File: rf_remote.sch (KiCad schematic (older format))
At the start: 21 parts, among them J1 10118194-0001LF, P1 CONN_01X04, P2 CONN_01X01, U1 SAMD21E18, U2 RFM69CW-915MHZ, U3 MIC5504-3.3YM5-T5

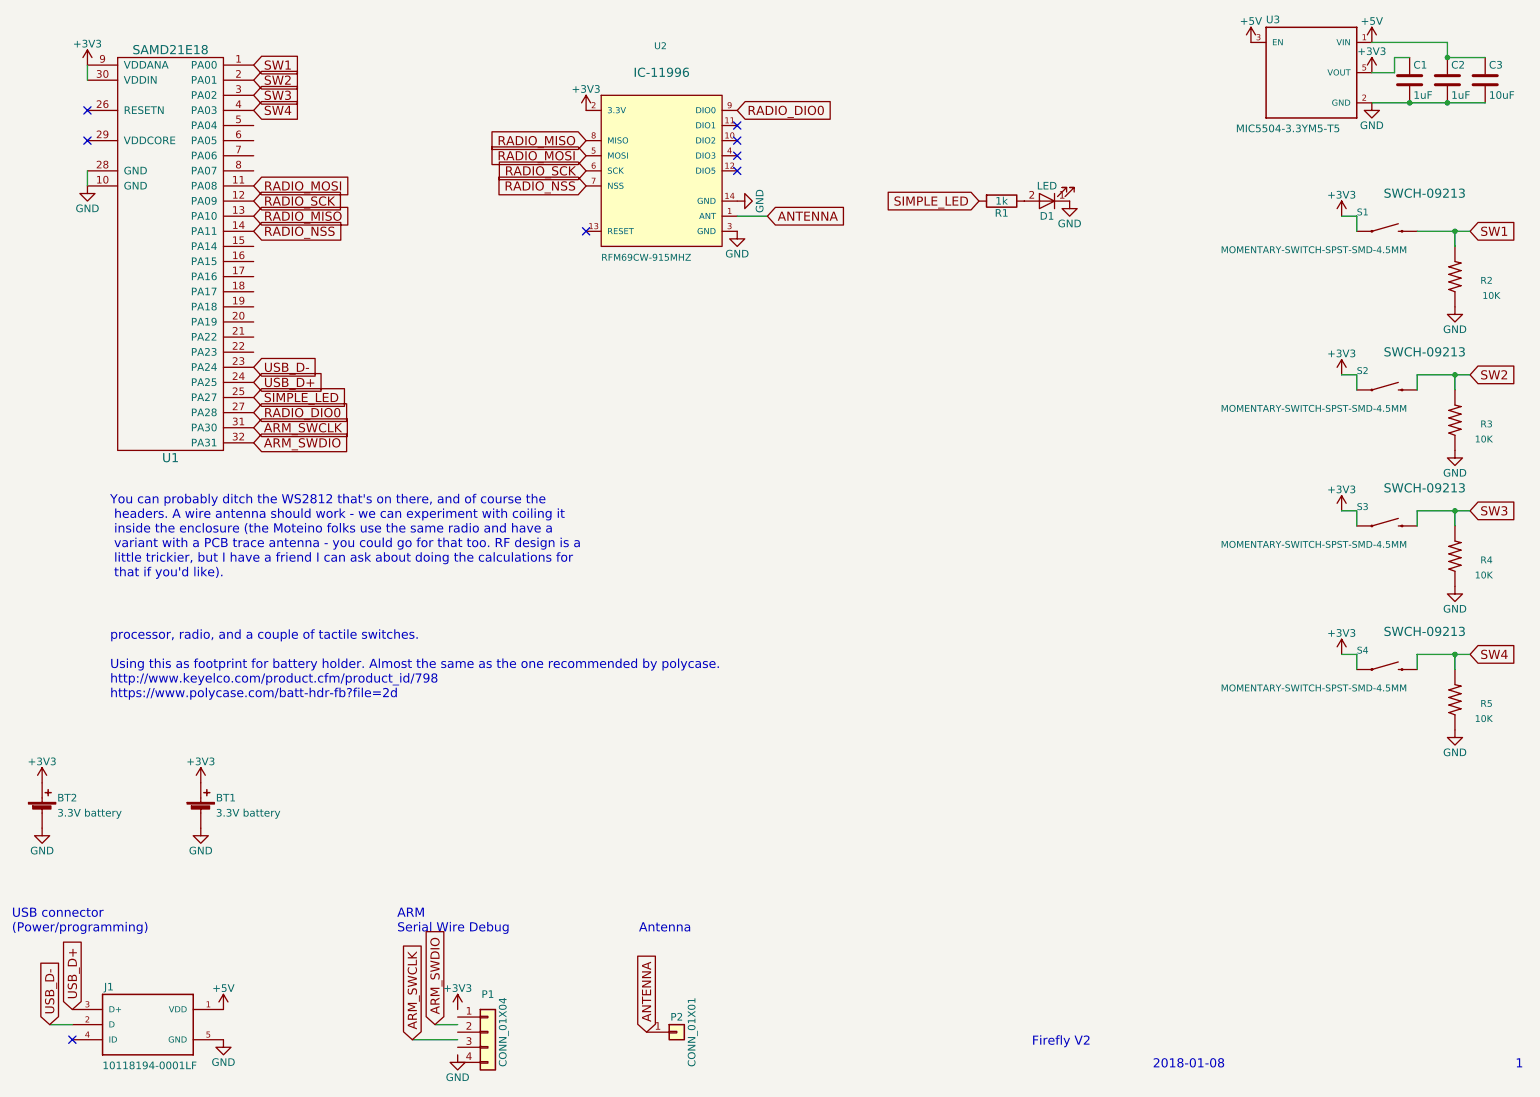
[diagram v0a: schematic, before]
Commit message: Removed second battery, updated PCB layout
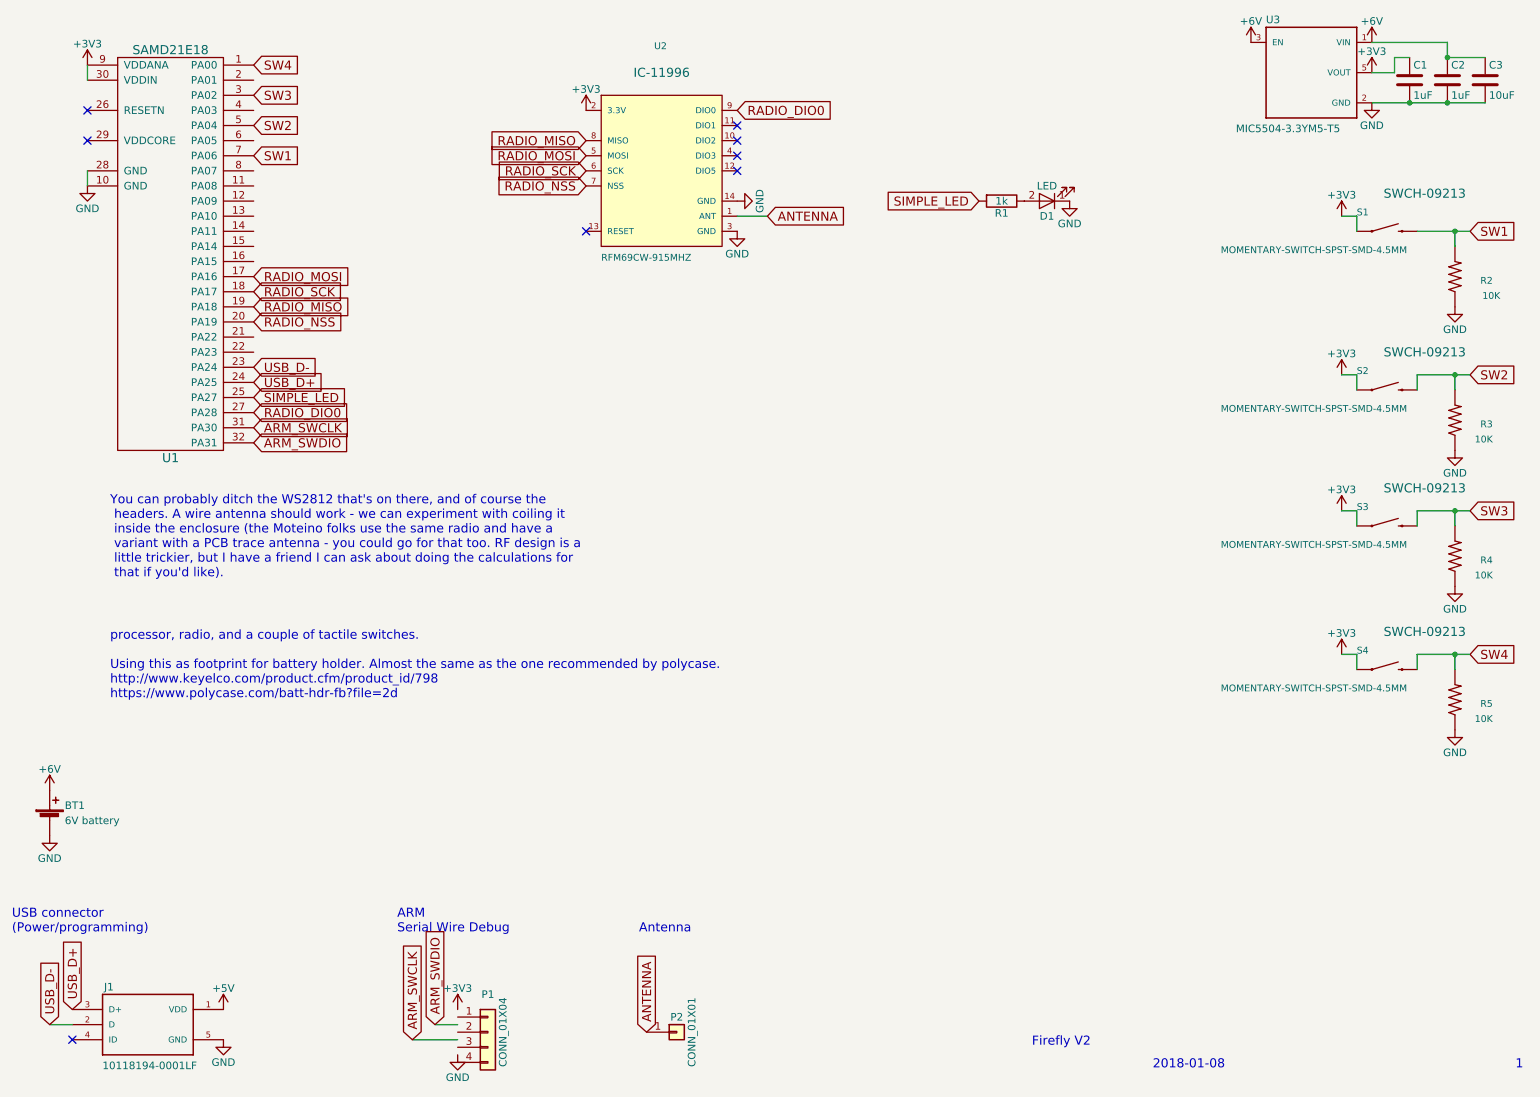
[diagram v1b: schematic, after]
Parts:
- removed BT2: 3.3V battery, Battery_Holders:Keystone_3034_1x20mm-CoinCell, symbol Battery_Cell
- BT1: value 3.3V battery -> 6V battery
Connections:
- net labels added: +6V
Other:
- moved on the sheet: BT1
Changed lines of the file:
@@
 $EndComp
 $Comp
-L +5V #PWR08
-U 1 1 5A547413
-P 8800 850
-F 0 "#PWR08" H 8800 700 50  0001 C CNN
-F 1 "+5V" H 8800 990 50  0000 C CNN
-F 2 "" H 8800 850 50  0000 C CNN
-F 3 "" H 8800 850 50  0000 C CNN
-	1    8800 850
-	1    0    0    -1
-$EndComp
-$Comp
-L +3V3 #PWR09
+L +3V3 #PWR08
 U 1 1 5A547441
 P 9600 1050
-F 0 "#PWR09" H 9600 900 50  0001 C CNN
+F 0 "#PWR08" H 9600 900 50  0001 C CNN
 F 1 "+3V3" H 9600 1190 50  0000 C CNN
 F 2 "" H 9600 1050 50  0000 C CNN
@@
 $EndComp
 $Comp
-L +3V3 #PWR010
+L +3V3 #PWR09
 U 1 1 5A54A758
 P 4400 1300
-F 0 "#PWR010" H 4400 1150 50  0001 C CNN
+F 0 "#PWR09" H 4400 1150 50  0001 C CNN
 F 1 "+3V3" H 4400 1440 50  0000 C CNN
 F 2 "" H 4400 1300 50  0000 C CNN
@@
 $EndComp
 $Comp
-L +5V #PWR011
-U 1 1 5A84FAAB
-P 9600 850
-F 0 "#PWR011" H 9600 700 50  0001 C CNN
-F 1 "+5V" H 9600 990 50  0000 C CNN
-F 2 "" H 9600 850 50  0000 C CNN
-F 3 "" H 9600 850 50  0000 C CNN
-	1    9600 850
-	1    0    0    -1
-$EndComp
-$Comp
 L C C1
 U 1 1 5A84FB7B
@@
 $EndComp
 $Comp
-L +3V3 #PWR012
+L +3V3 #PWR010
 U 1 1 5A851BC3
 P 1100 1000
-F 0 "#PWR012" H 1100 850 50  0001 C CNN
+F 0 "#PWR010" H 1100 850 50  0001 C CNN
 F 1 "+3V3" H 1100 1140 50  0000 C CNN
 F 2 "" H 1100 1000 50  0001 C CNN
@@
 	1100 1100 1100 1000
 $Comp
-L GND #PWR013
+L GND #PWR011
 U 1 1 5A851C44
 P 1100 1800
-F 0 "#PWR013" H 1100 1550 50  0001 C CNN
+F 0 "#PWR011" H 1100 1550 50  0001 C CNN
 F 1 "GND" H 1100 1650 50  0000 C CNN
 F 2 "" H 1100 1800 50  0001 C CNN
@@
 Text GLabel 2200 3100 2    60   Input ~ 0
 USB_D+
-Text GLabel 2200 1800 2    60   Input ~ 0
+Text GLabel 2200 2400 2    60   Input ~ 0
 RADIO_MOSI
-Text GLabel 2200 1900 2    60   Input ~ 0
+Text GLabel 2200 2500 2    60   Input ~ 0
 RADIO_SCK
-Text GLabel 2200 2000 2    60   Input ~ 0
+Text GLabel 2200 2600 2    60   Input ~ 0
 RADIO_MISO
-Text GLabel 2200 2100 2    60   Input ~ 0
+Text GLabel 2200 2700 2    60   Input ~ 0
 RADIO_NSS
 Text GLabel 2200 3200 2    60   Input ~ 0
@@
 SIMPLE_LED
 $Comp
-L GND #PWR014
+L GND #PWR012
 U 1 1 5A853737
 P 7600 1900
-F 0 "#PWR014" H 7600 1650 50  0001 C CNN
+F 0 "#PWR012" H 7600 1650 50  0001 C CNN
 F 1 "GND" H 7600 1750 50  0000 C CNN
 F 2 "" H 7600 1900 50  0000 C CNN
@@
 Text Notes 1250 5200 0    60   ~ 0
 processor, radio, and a couple of tactile switches.\n\nUsing this as footprint for battery holder. Almost the same as the one recommended by polycase.\nhttp://www.keyelco.com/product.cfm/product_id/798\nhttps://www.polycase.com/batt-hdr-fb?file=2d
-Text GLabel 2200 1000 2    60   Input ~ 0
+Text GLabel 2200 1600 2    60   Input ~ 0
 SW1
 Text GLabel 10250 2100 2    60   Input ~ 0
 SW1
-Text GLabel 2200 1100 2    60   Input ~ 0
+Text GLabel 2200 1400 2    60   Input ~ 0
 SW2
 Text GLabel 2200 1200 2    60   Input ~ 0
 SW3
-Text GLabel 2200 1300 2    60   Input ~ 0
+Text GLabel 2200 1000 2    60   Input ~ 0
 SW4
 Text GLabel 10250 3050 2    60   Input ~ 0
@@
 SW4
 $Comp
-L GND #PWR015
+L GND #PWR013
 U 1 1 5ADD2C56
 P 10150 2600
-F 0 "#PWR015" H 10150 2350 50  0001 C CNN
+F 0 "#PWR013" H 10150 2350 50  0001 C CNN
 F 1 "GND" H 10150 2450 50  0000 C CNN
 F 2 "" H 10150 2600 50  0001 C CNN
@@
 Connection ~ 10150 4900
 $Comp
-L +3V3 #PWR016
+L +3V3 #PWR014
 U 1 1 5ADD30DC
 P 9400 2000
-F 0 "#PWR016" H 9400 1850 50  0001 C CNN
+F 0 "#PWR014" H 9400 1850 50  0001 C CNN
 F 1 "+3V3" H 9400 2140 50  0000 C CNN
 F 2 "" H 9400 2000 50  0001 C CNN
@@
 $EndComp
 $Comp
-L +3V3 #PWR017
+L +3V3 #PWR015
 U 1 1 5ADD3146
 P 9400 3050
-F 0 "#PWR017" H 9400 2900 50  0001 C CNN
+F 0 "#PWR015" H 9400 2900 50  0001 C CNN
 F 1 "+3V3" H 9400 3190 50  0000 C CNN
 F 2 "" H 9400 3050 50  0001 C CNN
@@
 $EndComp
 $Comp
-L +3V3 #PWR018
+L +3V3 #PWR016
 U 1 1 5ADD318A
 P 9400 3950
-F 0 "#PWR018" H 9400 3800 50  0001 C CNN
+F 0 "#PWR016" H 9400 3800 50  0001 C CNN
 F 1 "+3V3" H 9400 4090 50  0000 C CNN
 F 2 "" H 9400 3950 50  0001 C CNN
@@
 $EndComp
 $Comp
-L +3V3 #PWR019
+L +3V3 #PWR017
 U 1 1 5ADD31CE
 P 9400 4900
-F 0 "#PWR019" H 9400 4750 50  0001 C CNN
+F 0 "#PWR017" H 9400 4750 50  0001 C CNN
 F 1 "+3V3" H 9400 5040 50  0000 C CNN
 F 2 "" H 9400 4900 50  0001 C CNN
@@
 $EndComp
 $Comp
-L GND #PWR020
+L GND #PWR018
 U 1 1 5ADD4016
 P 10150 3550
-F 0 "#PWR020" H 10150 3300 50  0001 C CNN
+F 0 "#PWR018" H 10150 3300 50  0001 C CNN
 F 1 "GND" H 10150 3400 50  0000 C CNN
 F 2 "" H 10150 3550 50  0001 C CNN
@@
 $EndComp
 $Comp
-L GND #PWR021
+L GND #PWR019
 U 1 1 5ADD418C
 P 10150 4450
-F 0 "#PWR021" H 10150 4200 50  0001 C CNN
+F 0 "#PWR019" H 10150 4200 50  0001 C CNN
 F 1 "GND" H 10150 4300 50  0000 C CNN
 F 2 "" H 10150 4450 50  0001 C CNN
@@
 $EndComp
 $Comp
-L GND #PWR022
+L GND #PWR020
 U 1 1 5ADD4235
 P 10150 5400
-F 0 "#PWR022" H 10150 5150 50  0001 C CNN
+F 0 "#PWR020" H 10150 5150 50  0001 C CNN
 F 1 "GND" H 10150 5250 50  0000 C CNN
 F 2 "" H 10150 5400 50  0001 C CNN
@@
 L Battery_Cell BT1
 U 1 1 5ADD440D
-P 1850 5950
-F 0 "BT1" H 1950 6050 50  0000 L CNN
-F 1 "3.3V battery" H 1950 5950 50  0000 L CNN
-F 2 "Battery_Holders:Keystone_3034_1x20mm-CoinCell" V 1850 6010 50  0001 C CNN
-F 3 "" V 1850 6010 50  0001 C CNN
-	1    1850 5950
-	1    0    0    -1
-$EndComp
-$Comp
-L GND #PWR023
+P 850 6000
+F 0 "BT1" H 950 6100 50  0000 L CNN
+F 1 "6V battery" H 950 6000 50  0000 L CNN
+F 2 "Battery_Holders:Keystone_3034_1x20mm-CoinCell" V 850 6060 50  0001 C CNN
+F 3 "" V 850 6060 50  0001 C CNN
+	1    850  6000
+	1    0    0    -1
+$EndComp
+$Comp
+L GND #PWR021
 U 1 1 5ADD460D
-P 1850 6050
-F 0 "#PWR023" H 1850 5800 50  0001 C CNN
-F 1 "GND" H 1850 5900 50  0000 C CNN
-F 2 "" H 1850 6050 50  0001 C CNN
-F 3 "" H 1850 6050 50  0001 C CNN
-	1    1850 6050
-	1    0    0    -1
-$EndComp
-$Comp
-L +3V3 #PWR024
-U 1 1 5ADD465D
-P 1850 5750
-F 0 "#PWR024" H 1850 5600 50  0001 C CNN
-F 1 "+3V3" H 1850 5890 50  0000 C CNN
-F 2 "" H 1850 5750 50  0001 C CNN
-F 3 "" H 1850 5750 50  0001 C CNN
-	1    1850 5750
-	1    0    0    -1
-$EndComp
-$Comp
-L Battery_Cell BT2
-U 1 1 5B0336AD
-P 800 5950
-F 0 "BT2" H 900 6050 50  0000 L CNN
-F 1 "3.3V battery" H 900 5950 50  0000 L CNN
-F 2 "Battery_Holders:Keystone_3034_1x20mm-CoinCell" V 800 6010 50  0001 C CNN
-F 3 "" V 800 6010 50  0001 C CNN
-	1    800  5950
-	1    0    0    -1
-$EndComp
-$Comp
-L GND #PWR025
-U 1 1 5B0336B3
-P 800 6050
-F 0 "#PWR025" H 800 5800 50  0001 C CNN
-F 1 "GND" H 800 5900 50  0000 C CNN
-F 2 "" H 800 6050 50  0001 C CNN
-F 3 "" H 800 6050 50  0001 C CNN
-	1    800  6050
-	1    0    0    -1
-$EndComp
-$Comp
-L +3V3 #PWR026
-U 1 1 5B0336B9
-P 800 5750
-F 0 "#PWR026" H 800 5600 50  0001 C CNN
-F 1 "+3V3" H 800 5890 50  0000 C CNN
-F 2 "" H 800 5750 50  0001 C CNN
-F 3 "" H 800 5750 50  0001 C CNN
-	1    800  5750
+P 850 6100
+F 0 "#PWR021" H 850 5850 50  0001 C CNN
+F 1 "GND" H 850 5950 50  0000 C CNN
+F 2 "" H 850 6100 50  0001 C CNN
+F 3 "" H 850 6100 50  0001 C CNN
+	1    850  6100
 	1    0    0    -1
 $EndComp
@@
 	1    0    0    -1
 $EndComp
+$Comp
+L +6V #PWR022
+U 1 1 5B06356F
+P 8800 850
+F 0 "#PWR022" H 8800 700 50  0001 C CNN
+F 1 "+6V" H 8800 990 50  0000 C CNN
+F 2 "" H 8800 850 50  0000 C CNN
+F 3 "" H 8800 850 50  0000 C CNN
+	1    8800 850
+	1    0    0    -1
+$EndComp
+$Comp
+L +6V #PWR023
+U 1 1 5B063684
+P 9600 850
+F 0 "#PWR023" H 9600 700 50  0001 C CNN
+F 1 "+6V" H 9600 990 50  0000 C CNN
+F 2 "" H 9600 850 50  0000 C CNN
+F 3 "" H 9600 850 50  0000 C CNN
+	1    9600 850
+	1    0    0    -1
+$EndComp
+$Comp
+L +6V #PWR024
+U 1 1 5B063CC2
+P 850 5800
+F 0 "#PWR024" H 850 5650 50  0001 C CNN
+F 1 "+6V" H 850 5940 50  0000 C CNN
+F 2 "" H 850 5800 50  0000 C CNN
+F 3 "" H 850 5800 50  0000 C CNN
+	1    850  5800
+	1    0    0    -1
+$EndComp

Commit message: Removed linear reg & USB port. Draft of layout and routing.
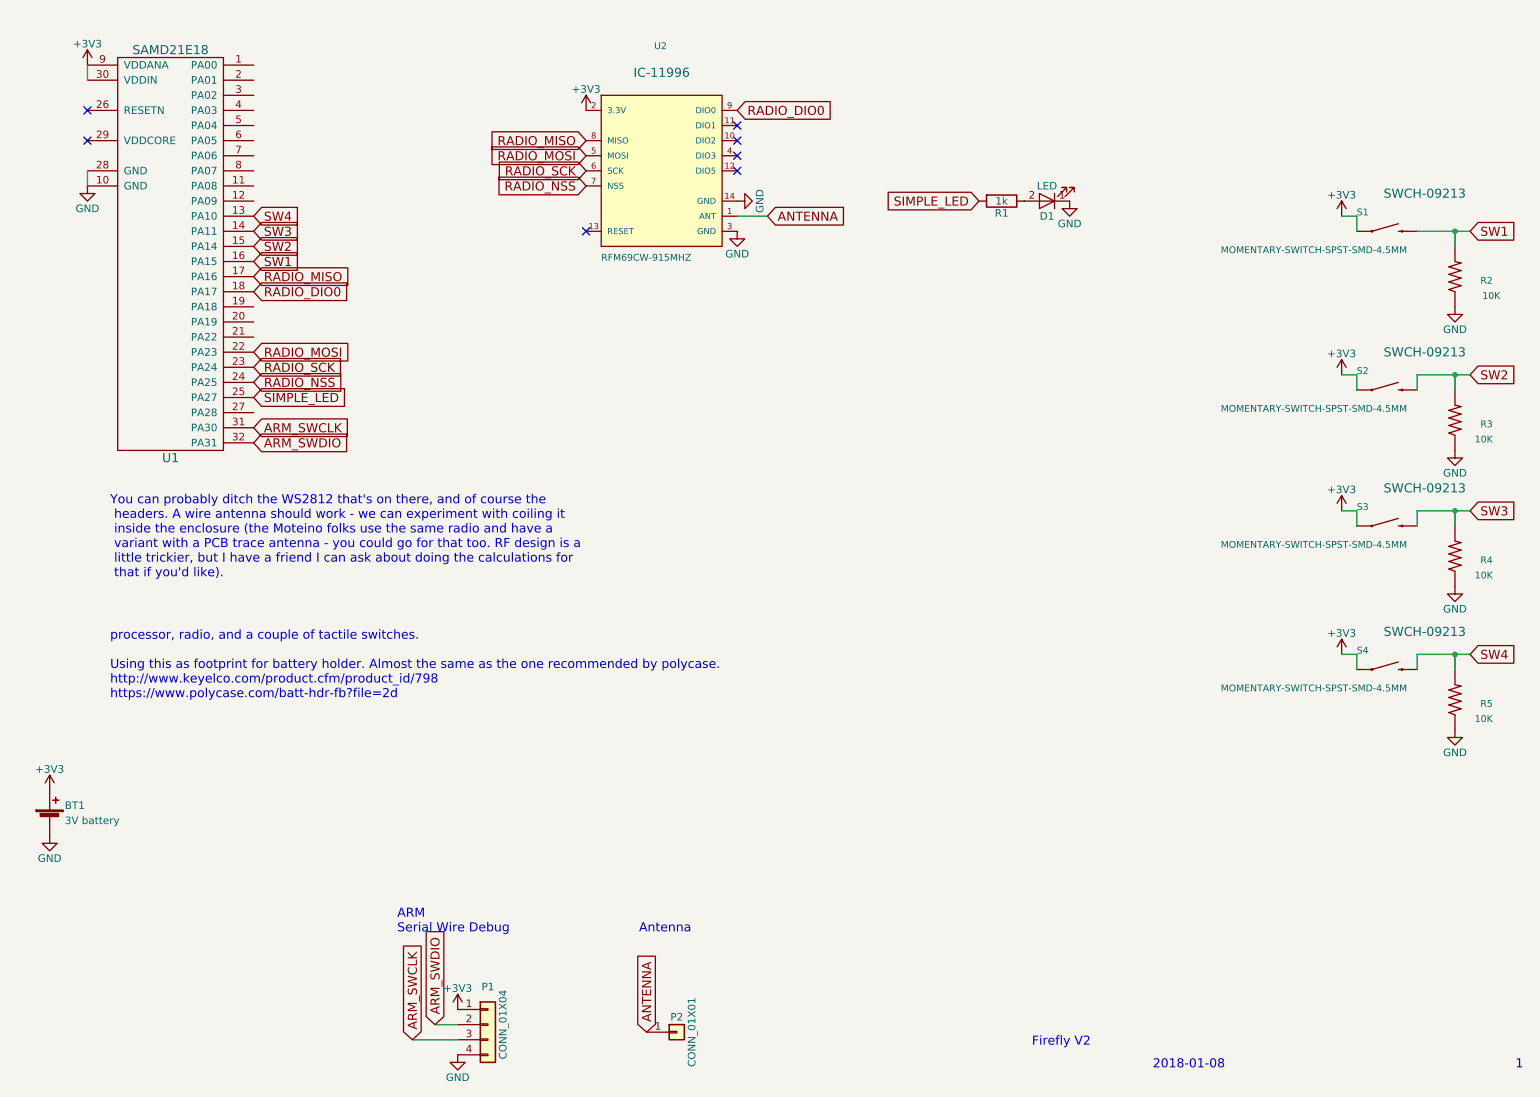
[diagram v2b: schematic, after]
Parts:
- removed C1, C2: 1uF, Capacitors_SMD:C_0603_HandSoldering, symbol C
- removed C3: 10uF, Capacitors_SMD:C_0805_HandSoldering, symbol C
- removed J1: 10118194-0001LF, 10118194-0001LF:FRAMATOME_10118194-0001LF, symbol 10118194-0001LF
- removed U3: MIC5504-3.3YM5-T5, MIC5504-3.3YM5-T5:SOT23-5P95_280X145XL45X37N, symbol MIC5504-3.3YM5-T5
- BT1: value 6V battery -> 3V battery
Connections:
- net labels removed: +5V, +6V, USB_D+, USB_D-
- wire segments 32 -> 24
- no-connect marks 8 -> 7
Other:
- note removed: "USB connector\n(Power/programming)"
- moved on the sheet: P1
